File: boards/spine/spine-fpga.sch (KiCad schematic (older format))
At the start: 29 parts, among them U7 iCE40-HX1K-TQ144

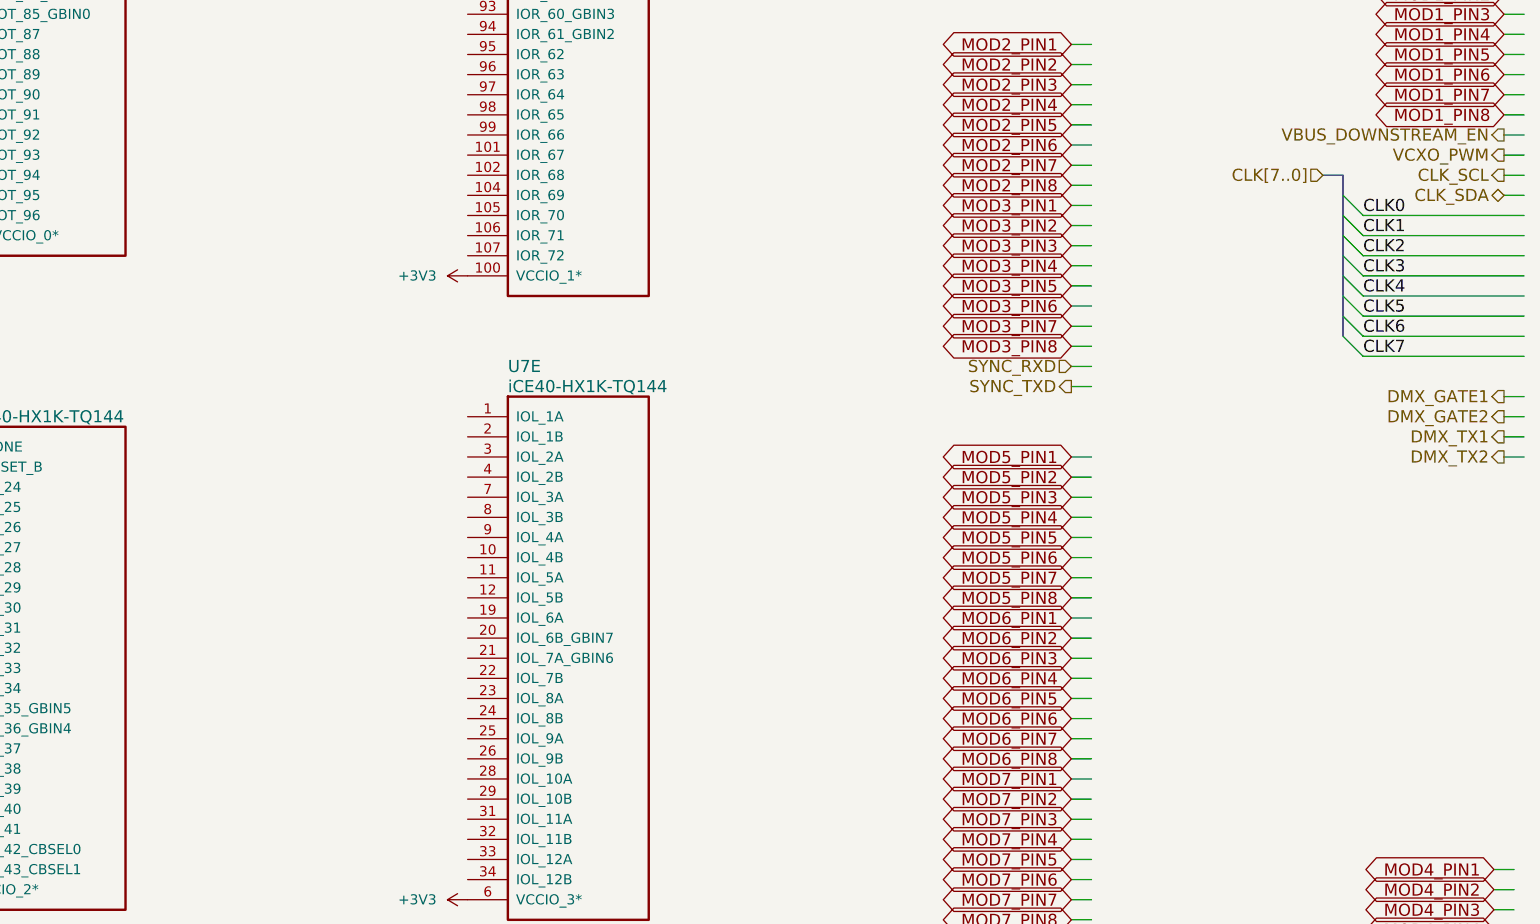
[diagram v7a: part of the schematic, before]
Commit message: Clock routing
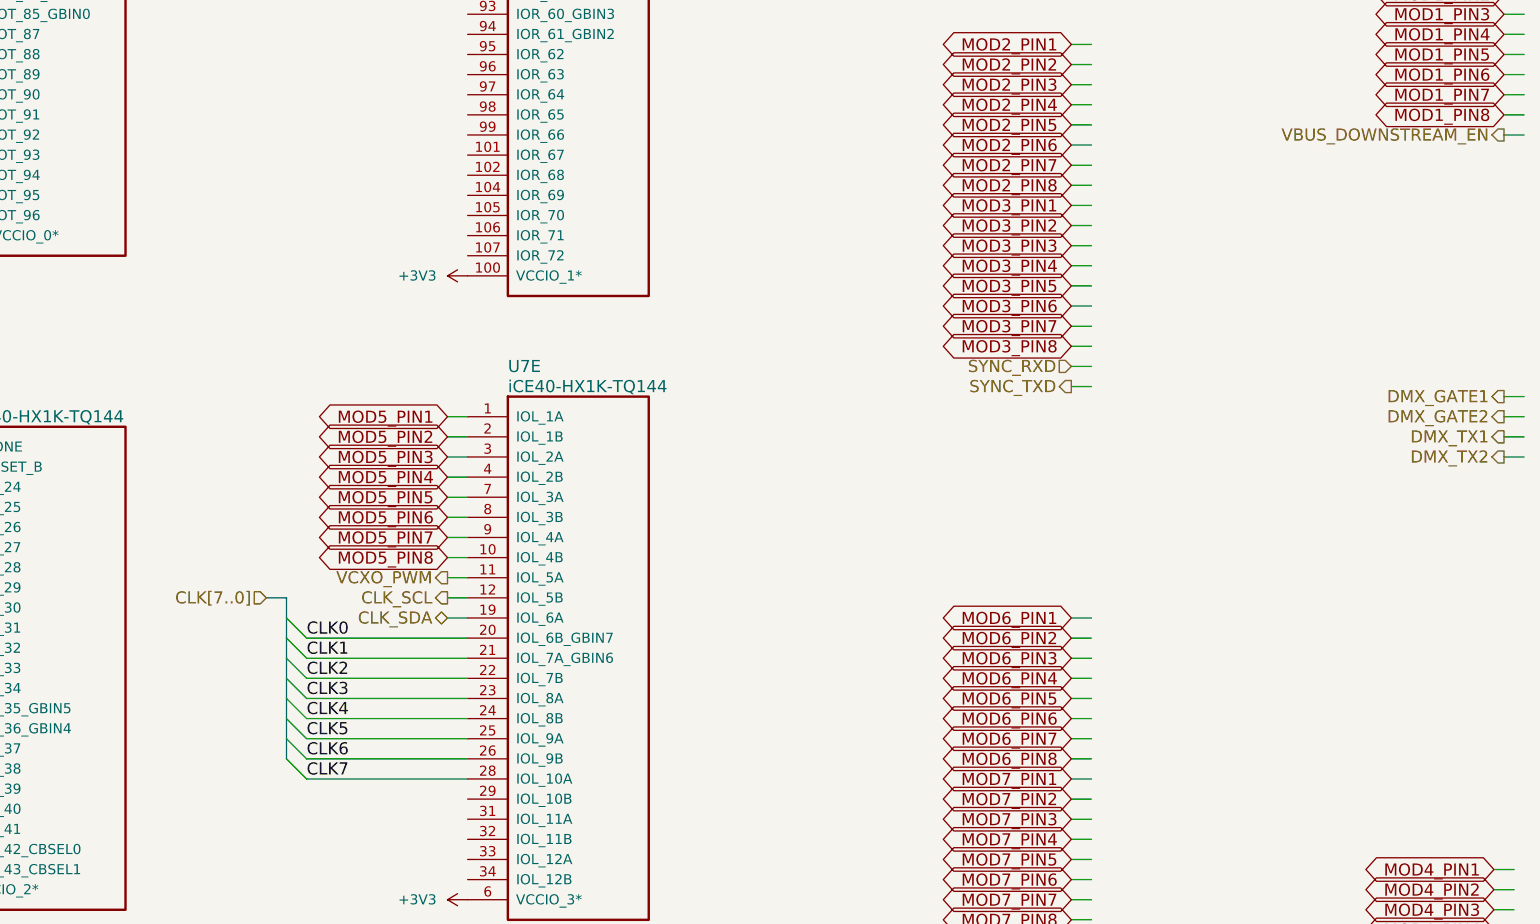
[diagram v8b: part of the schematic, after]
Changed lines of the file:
@@
 Text HLabel 12150 3950 0    60   Output ~ 0
 SYNC_TXD
-Text HLabel 14300 2900 0    60   Output ~ 0
+Text HLabel 9050 5000 0    60   Output ~ 0
 CLK_SCL
-Text HLabel 14300 3000 0    60   BiDi ~ 0
+Text HLabel 9050 5100 0    60   BiDi ~ 0
 CLK_SDA
-Text HLabel 14300 2800 0    60   Output ~ 0
+Text HLabel 9050 4900 0    60   Output ~ 0
 VCXO_PWM
-Text HLabel 13400 2900 0    60   Input ~ 0
+Text HLabel 8150 5000 0    60   Input ~ 0
 CLK[7..0]
 Wire Bus Line
@@
 	6350 6050 6450 6050
 Wire Bus Line
-	13400 2900 13500 2900
+	8150 5000 8250 5000
 Wire Bus Line
-	13500 2900 13500 3700
+	8250 5000 8250 5800
 Entry Wire Line
-	13500 3700 13600 3800
+	8250 5800 8350 5900
 Entry Wire Line
-	13500 3600 13600 3700
+	8250 5700 8350 5800
 Entry Wire Line
-	13500 3400 13600 3500
+	8250 5500 8350 5600
 Entry Wire Line
-	13500 3300 13600 3400
+	8250 5400 8350 5500
 Entry Wire Line
-	13500 3200 13600 3300
+	8250 5300 8350 5400
 Entry Wire Line
-	13500 3100 13600 3200
+	8250 5200 8350 5300
 Entry Wire Line
-	13500 3000 13600 3100
+	8250 5100 8350 5200
 Entry Wire Line
-	13500 3500 13600 3600
+	8250 5600 8350 5700
 Wire Wire Line
-	13600 3100 14400 3100
+	8350 5200 9150 5200
 Wire Wire Line
-	13600 3200 14400 3200
+	8350 5300 9150 5300
 Wire Wire Line
-	13600 3300 14400 3300
+	8350 5400 9150 5400
 Wire Wire Line
-	13600 3400 14400 3400
+	8350 5500 9150 5500
 Wire Wire Line
-	13600 3500 14400 3500
+	8350 5600 9150 5600
 Wire Wire Line
-	13600 3600 14400 3600
+	8350 5700 9150 5700
 Wire Wire Line
-	13600 3700 14400 3700
+	8350 5800 9150 5800
 Wire Wire Line
-	13600 3800 14400 3800
-Text Label 13600 3100 0    60   ~ 0
+	8350 5900 9150 5900
+Text Label 8350 5200 0    60   ~ 0
 CLK0
-Text Label 13600 3200 0    60   ~ 0
+Text Label 8350 5300 0    60   ~ 0
 CLK1
-Text Label 13600 3300 0    60   ~ 0
+Text Label 8350 5400 0    60   ~ 0
 CLK2
-Text Label 13600 3400 0    60   ~ 0
+Text Label 8350 5500 0    60   ~ 0
 CLK3
-Text Label 13600 3500 0    60   ~ 0
+Text Label 8350 5600 0    60   ~ 0
 CLK4
-Text Label 13600 3600 0    60   ~ 0
+Text Label 8350 5700 0    60   ~ 0
 CLK5
-Text Label 13600 3700 0    60   ~ 0
+Text Label 8350 5800 0    60   ~ 0
 CLK6
-Text Label 13600 3800 0    60   ~ 0
+Text Label 8350 5900 0    60   ~ 0
 CLK7
 Wire Wire Line
@@
 	14400 4300 14300 4300
 Wire Wire Line
-	14300 2800 14400 2800
+	9050 4900 9150 4900
 Wire Wire Line
-	14400 2900 14300 2900
+	9150 5000 9050 5000
 Wire Wire Line
-	14300 3000 14400 3000
+	9050 5100 9150 5100
 Text GLabel 14300 1900 0    60   BiDi ~ 0
 MOD1_PIN1
@@
 Text GLabel 14250 7050 0    60   BiDi ~ 0
 MOD4_PIN8
-Text GLabel 12150 4300 0    60   BiDi ~ 0
+Text GLabel 9050 4100 0    60   BiDi ~ 0
 MOD5_PIN1
-Text GLabel 12150 4400 0    60   BiDi ~ 0
+Text GLabel 9050 4200 0    60   BiDi ~ 0
 MOD5_PIN2
-Text GLabel 12150 4500 0    60   BiDi ~ 0
+Text GLabel 9050 4300 0    60   BiDi ~ 0
 MOD5_PIN3
-Text GLabel 12150 4700 0    60   BiDi ~ 0
+Text GLabel 9050 4500 0    60   BiDi ~ 0
 MOD5_PIN5
-Text GLabel 12150 4900 0    60   BiDi ~ 0
+Text GLabel 9050 4700 0    60   BiDi ~ 0
 MOD5_PIN7
-Text GLabel 12150 4600 0    60   BiDi ~ 0
+Text GLabel 9050 4400 0    60   BiDi ~ 0
 MOD5_PIN4
-Text GLabel 12150 4800 0    60   BiDi ~ 0
+Text GLabel 9050 4600 0    60   BiDi ~ 0
 MOD5_PIN6
-Text GLabel 12150 5000 0    60   BiDi ~ 0
+Text GLabel 9050 4800 0    60   BiDi ~ 0
 MOD5_PIN8
 Text GLabel 12150 5100 0    60   BiDi ~ 0
@@
 	12150 3750 12250 3750
 Wire Wire Line
-	12150 4300 12250 4300
+	9050 4100 9150 4100
 Wire Wire Line
-	12150 4500 12250 4500
+	9050 4300 9150 4300
 Wire Wire Line
-	12150 4700 12250 4700
+	9050 4500 9150 4500
 Wire Wire Line
-	12150 4900 12250 4900
+	9050 4700 9150 4700
 Wire Wire Line
-	12150 4400 12250 4400
+	9050 4200 9150 4200
 Wire Wire Line
-	12150 4600 12250 4600
+	9050 4400 9150 4400
 Wire Wire Line
-	12150 4800 12250 4800
+	9050 4600 9150 4600
 Wire Wire Line
-	12150 5000 12250 5000
+	9050 4800 9150 4800
 Wire Wire Line
 	14250 6350 14350 6350
@@
 FB 59 00 E6 A5 69 3A 37 9E CF 73 BC F7 37 E3 33 5D 9E A8 3E 7F 80 FA F7 F6 BB 44 F4 6E D4 E7 77
 A2 1E 1F 27 A2 E3 16 70 32 E9 54 FE 3F E7 AF 00 CA 1C A3 36 0A 00 00 00 00 49 45 4E 44 AE 42 60
-82 70
+82 FF
 EndData
 $EndBitmap
@@
 72 0F 1C A9 DC 70 49 CB 79 33 88 85 99 AD 01 6C 4B 10 FC 3B 13 DE 3B 37 68 79 AD 07 BC 00 3C 0E
 3C 31 EE E3 D8 E7 0F 03 D7 7B 9F FB C1 E1 FF 01 18 C4 96 1D B8 0E 40 07 00 00 00 00 49 45 4E 44
-AE 42 60 82 F9
+AE 42 60 82 00
 EndData
 $EndBitmap
@@
 FB 59 00 E6 A5 69 3A 37 9E CF 73 BC F7 37 E3 33 5D 9E A8 3E 7F 80 FA F7 F6 BB 44 F4 6E D4 E7 77
 A2 1E 1F 27 A2 E3 16 70 32 E9 54 FE 3F E7 AF 00 CA 1C A3 36 0A 00 00 00 00 49 45 4E 44 AE 42 60
-82 FE
+82 FF
 EndData
 $EndBitmap
